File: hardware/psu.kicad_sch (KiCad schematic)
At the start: 35 parts, among them J6 Screw_Terminal_01x02, J7 Barrel_Jack_MountingPin, Q1 FDS4435BZ, U5 NCP1117-3.3_SOT223, U6 AP64501SP-13

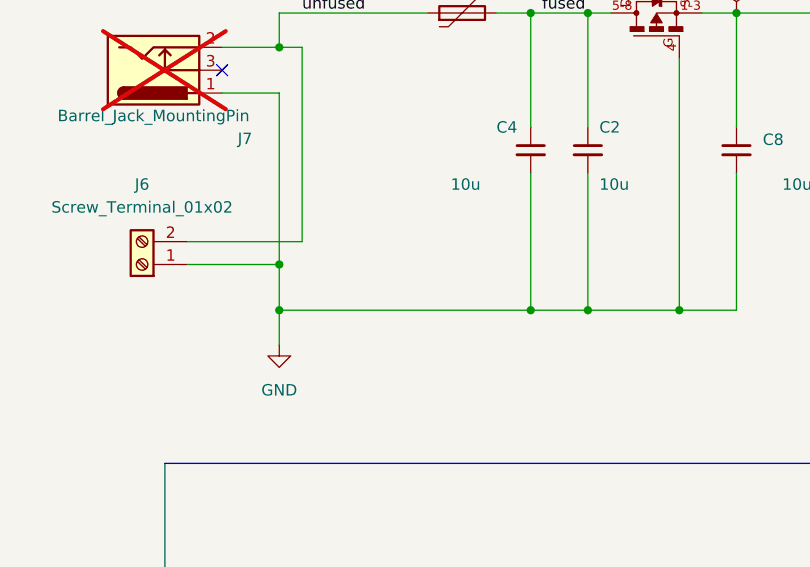
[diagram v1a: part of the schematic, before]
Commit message: Clean up ERC: PWR_FLAGs, OTG_ID solder jumper, PCIe_CLK_nREQ
- Add PWR_FLAG on GND net (PSU sheet)
- USB_OTG_ID: solder jumper to GND with 10K pull-up for host/device mode
- PCIe_CLK_nREQ tied to GND locally on connector 2
- 1 ERC error remaining: CM4 dual 3.3V output pins (false positive)
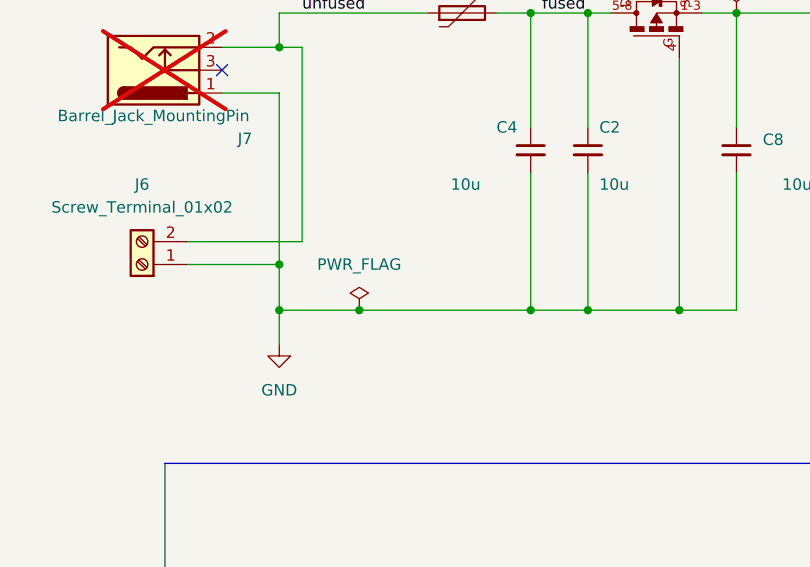
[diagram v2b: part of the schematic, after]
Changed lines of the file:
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@@
 	)
 	(junction
+		(at 60.96 77.47)
+		(diameter 0)
+		(color 0 0 0 0)
+	)
+	(junction
 		(at 218.44 113.03)
 		(diameter 0)
@@
 	(wire
 		(pts
-			(xy 52.07 77.47) (xy 80.01 77.47)
+			(xy 52.07 77.47) (xy 60.96 77.47)
 		)
 		(stroke
@@
 	(wire
 		(pts
+			(xy 237.49 48.26) (xy 247.65 48.26)
+		)
+		(stroke
+			(width 0)
+			(type default)
+		)
+	)
+	(wire
+		(pts
 			(xy 76.2 127) (xy 86.36 127)
 		)
@@
 	(wire
 		(pts
-			(xy 237.49 48.26) (xy 247.65 48.26)
-		)
-		(stroke
-			(width 0)
-			(type default)
-		)
-	)
-	(wire
-		(pts
 			(xy 228.6 120.65) (xy 237.49 120.65)
 		)
@@
 	(wire
 		(pts
+			(xy 60.96 77.47) (xy 80.01 77.47)
+		)
+		(stroke
+			(width 0)
+			(type default)
+		)
+	)
+	(wire
+		(pts
 			(xy 86.36 127) (xy 86.36 128.27)
 		)
@@
 					(unit 1)
 				)
+			)
+		)
+	)
+	(symbol
+		(lib_id "power:PWR_FLAG")
+		(at 60.96 77.47 0)
+		(unit 1)
+		(body_style 1)
+		(exclude_from_sim no)
+		(in_bom yes)
+		(on_board yes)
+		(in_pos_files yes)
+		(dnp no)
+		(fields_autoplaced yes)
+		(property "Reference" "#FLG05"
+			(at 60.96 75.565 0)
+			(hide yes)
+			(show_name no)
+			(do_not_autoplace no)
+			(effects
+				(font
+					(size 1.27 1.27)
+				)
+			)
+		)
+		(property "Value" "PWR_FLAG"
+			(at 60.96 72.39 0)
+			(show_name no)
+			(do_not_autoplace no)
+			(effects
+				(font
+					(size 1.27 1.27)
+				)
+			)
+		)
+		(property "Footprint" ""
+			(at 60.96 77.47 0)
+			(hide yes)
+			(show_name no)
+			(do_not_autoplace no)
+			(effects
+				(font
+					(size 1.27 1.27)
+				)
+			)
+		)
+		(property "Datasheet" ""
+			(at 60.96 77.47 0)
+			(hide yes)
+			(show_name no)
+			(do_not_autoplace no)
+			(effects
+				(font
+					(size 1.27 1.27)
+				)
+			)
+		)
+		(property "Description" "Special symbol for telling ERC where power comes from"
+			(at 60.96 77.47 0)
+			(hide yes)
+			(show_name no)
+			(do_not_autoplace no)
+			(effects
+				(font
+					(size 1.27 1.27)
+				)
+			)
+		)
+		(pin "1"
+		)
+		(instances
+			(project "granit"
+				(path "/d2c135e3-a983-4cd4-8cff-b50ca3c7671a/5c34f141-50d5-4609-a101-f9d94643eff8"
+					(reference "#FLG05")
+					(unit 1)
+				)

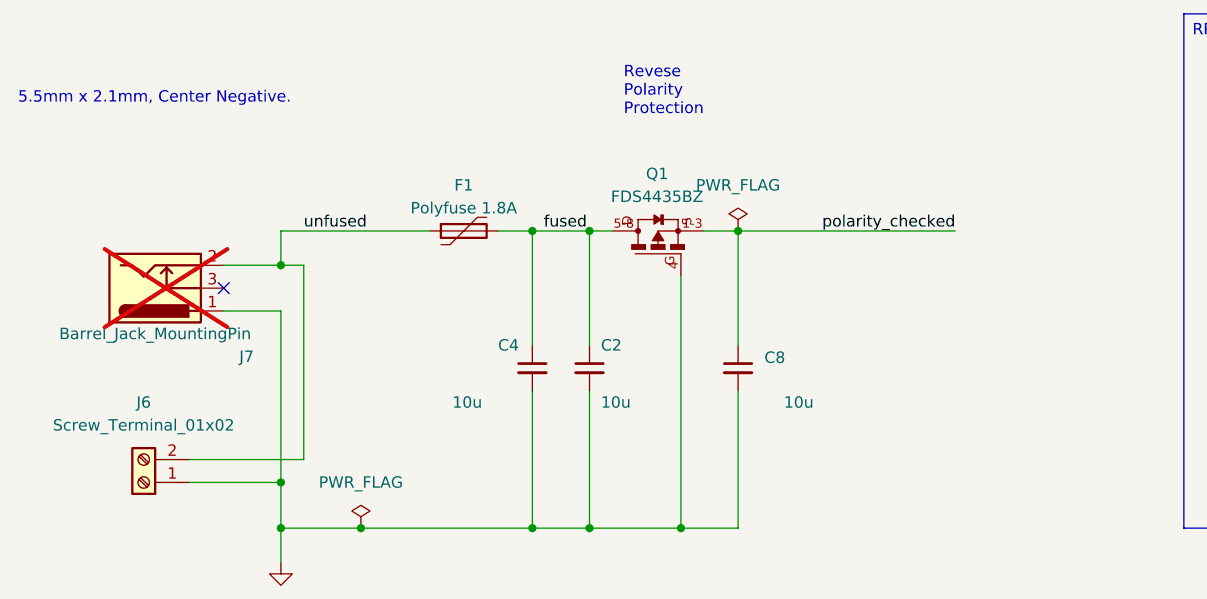
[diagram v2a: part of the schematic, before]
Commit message: SATA: add power connector (12V, 5V, 3.3V, GND)
- 12V passthrough from PSU (after polarity protection)
- 5V from AP64501SP-13 buck
- 3.3V from NCP1117 LDO (for completeness)
- FIXME: TPM/crypto chip added to TODO
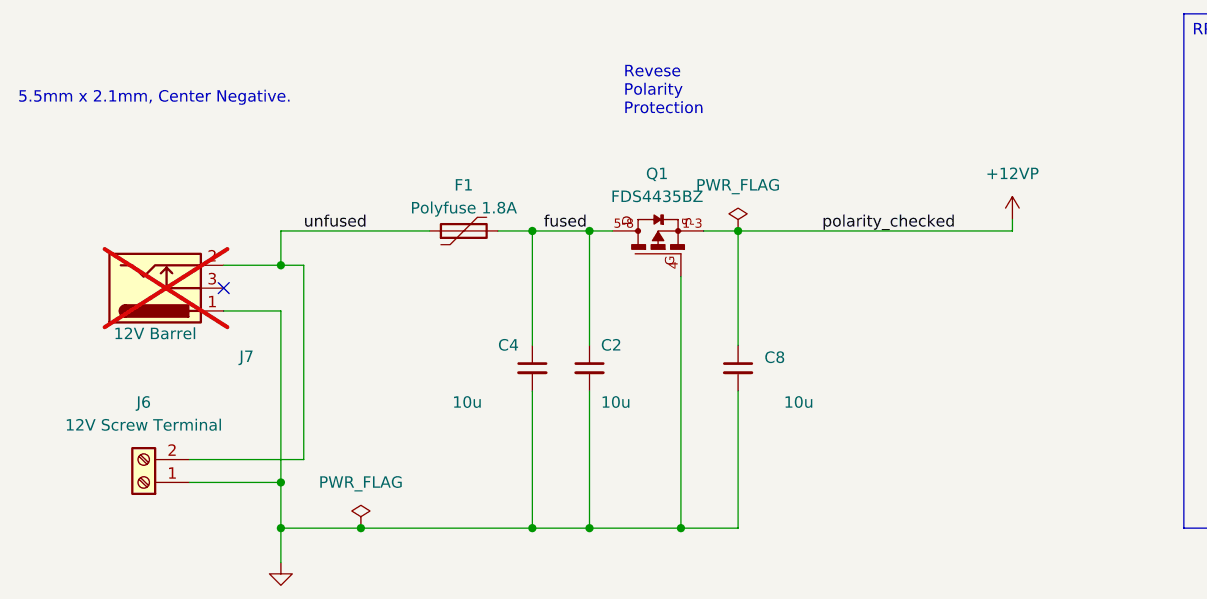
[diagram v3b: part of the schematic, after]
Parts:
- J6: value Screw_Terminal_01x02 -> 12V Screw Terminal
- J7: value Barrel_Jack_MountingPin -> 12V Barrel
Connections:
- net polarity_checked renamed +12VP
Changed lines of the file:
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@@
 		)
 	)
+	(wire
+		(pts
+			(xy 133.35 43.18) (xy 133.35 44.45)
+		)
+		(stroke
+			(width 0)
+			(type default)
+		)
+	)
 	(polyline
 		(pts
@@
 	(wire
 		(pts
-			(xy 102.87 44.45) (xy 127 44.45)
+			(xy 102.87 44.45) (xy 133.35 44.45)
 		)
 		(stroke
@@
 			)
 		)
-		(property "Value" "Screw_Terminal_01x02"
+		(property "Value" "12V Screw Terminal"
 			(at 36.83 66.04 0)
 			(show_name no)
@@
 			)
 		)
-		(property "Value" "Barrel_Jack_MountingPin"
+		(property "Value" "12V Barrel"
 			(at 38.1 55.88 0)
 			(show_name no)
@@
 					(unit 1)
 				)
+			)
+		)
+	)
+	(symbol
+		(lib_id "power:+12V")
+		(at 133.35 43.18 0)
+		(unit 1)
+		(body_style 1)
+		(exclude_from_sim no)
+		(in_bom yes)
+		(on_board yes)
+		(in_pos_files yes)
+		(dnp no)
+		(fields_autoplaced yes)
+		(property "Reference" "#PWR068"
+			(at 133.35 46.99 0)
+			(hide yes)
+			(show_name no)
+			(do_not_autoplace no)
+			(effects
+				(font
+					(size 1.27 1.27)
+				)
+			)
+		)
+		(property "Value" "+12VP"
+			(at 133.35 38.1 0)
+			(show_name no)
+			(do_not_autoplace no)
+			(effects
+				(font
+					(size 1.27 1.27)
+				)
+			)
+		)
+		(property "Footprint" ""
+			(at 133.35 43.18 0)
+			(hide yes)
+			(show_name no)
+			(do_not_autoplace no)
+			(effects
+				(font
+					(size 1.27 1.27)
+				)
+			)
+		)
+		(property "Datasheet" ""
+			(at 133.35 43.18 0)
+			(hide yes)
+			(show_name no)
+			(do_not_autoplace no)
+			(effects
+				(font
+					(size 1.27 1.27)
+				)
+			)
+		)
+		(property "Description" "Power symbol creates a global label with name \"+12V\""
+			(at 133.35 43.18 0)
+			(hide yes)
+			(show_name no)
+			(do_not_autoplace no)
+			(effects
+				(font
+					(size 1.27 1.27)
+				)
+			)
+		)
+		(pin "1"
+		)
+		(instances
+			(project "granit"
+				(path "/d2c135e3-a983-4cd4-8cff-b50ca3c7671a/5c34f141-50d5-4609-a101-f9d94643eff8"
+					(reference "#PWR068")
+					(unit 1)
+				)
